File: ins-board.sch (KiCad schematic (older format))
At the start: 83 parts, among them Q1 FDN306P, U2 STM32F415RGT6, U6 LT1761-3.3, U7 LT1965, X1 CRYSTAL 16MHz 10ppm

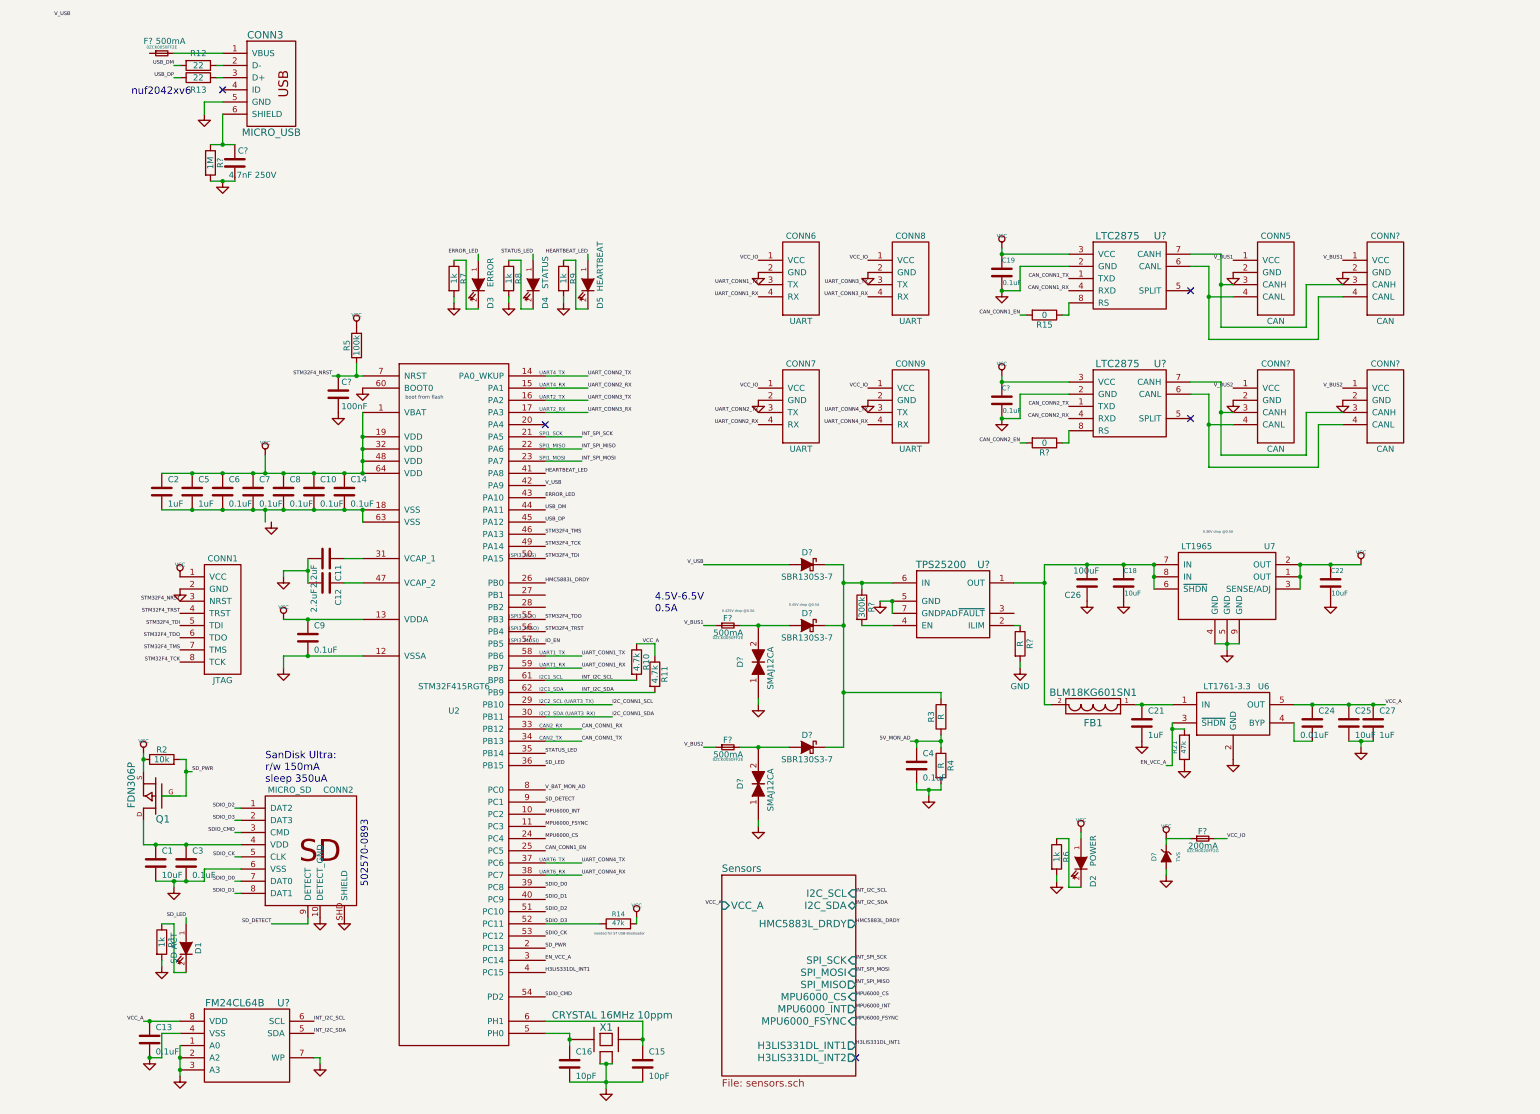
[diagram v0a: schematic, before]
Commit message: smaller esd protection
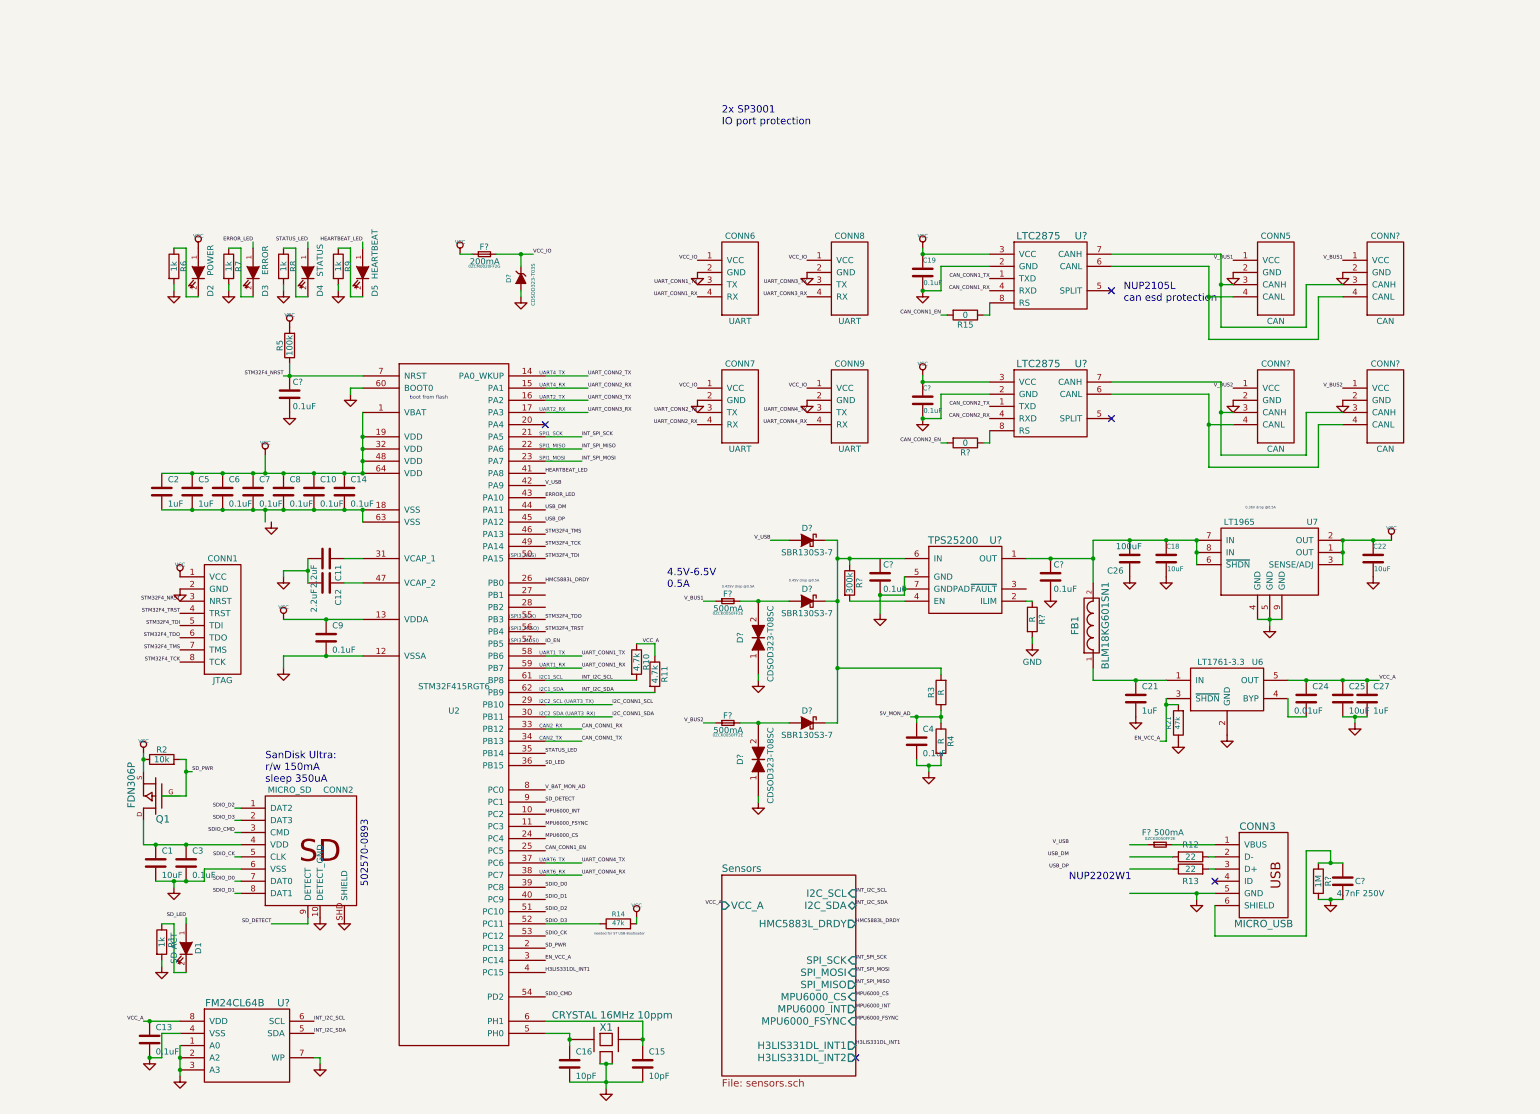
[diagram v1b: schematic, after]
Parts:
- removed D?: TVS, symbol ZENERsmall
- added C? (x2): 0.1uF, symbol C
- added D?: CDSOD323-T03S, symbol ZENERsmall
- C?: value 100nF -> 0.1uF
- D? (x2): value SMAJ12CA -> CDSOD323-T08SC
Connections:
- net GND: now also C?.2, C?.2, D?.1 (A)
- net USB_DM: no longer R12.2
- net USB_DP: no longer R13.1
- net VCC_IO: now also D?.2 (K)
- net at C18.1, C26.2, FB1.2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: now also C?.1
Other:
- note added: "2x SP3001\nIO port protection"
- note added: "NUP2105L \ncan esd protection"
- note added: "NUP2202W1"
- note removed: "nuf2042xv6"
- moved on the sheet: C18, C19, C21, C22, C24, C25, C26, C27, C4, C9, C?, CONN3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

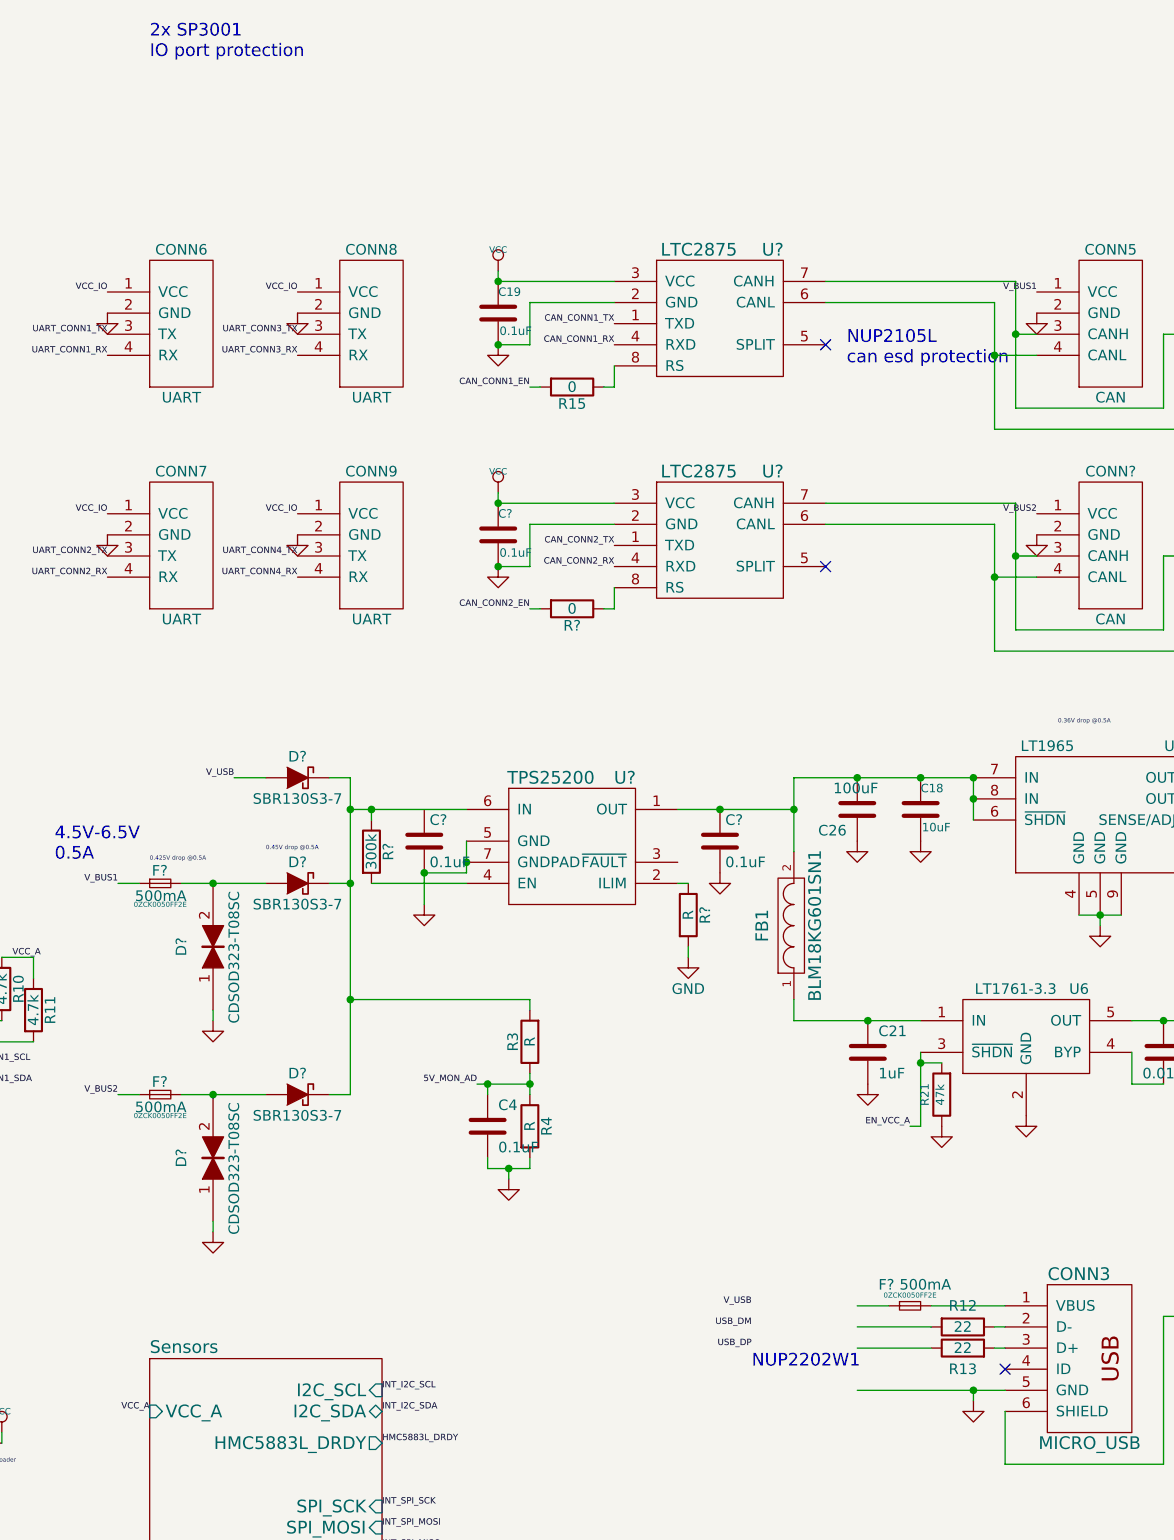
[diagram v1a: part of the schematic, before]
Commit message: USB ESD protection
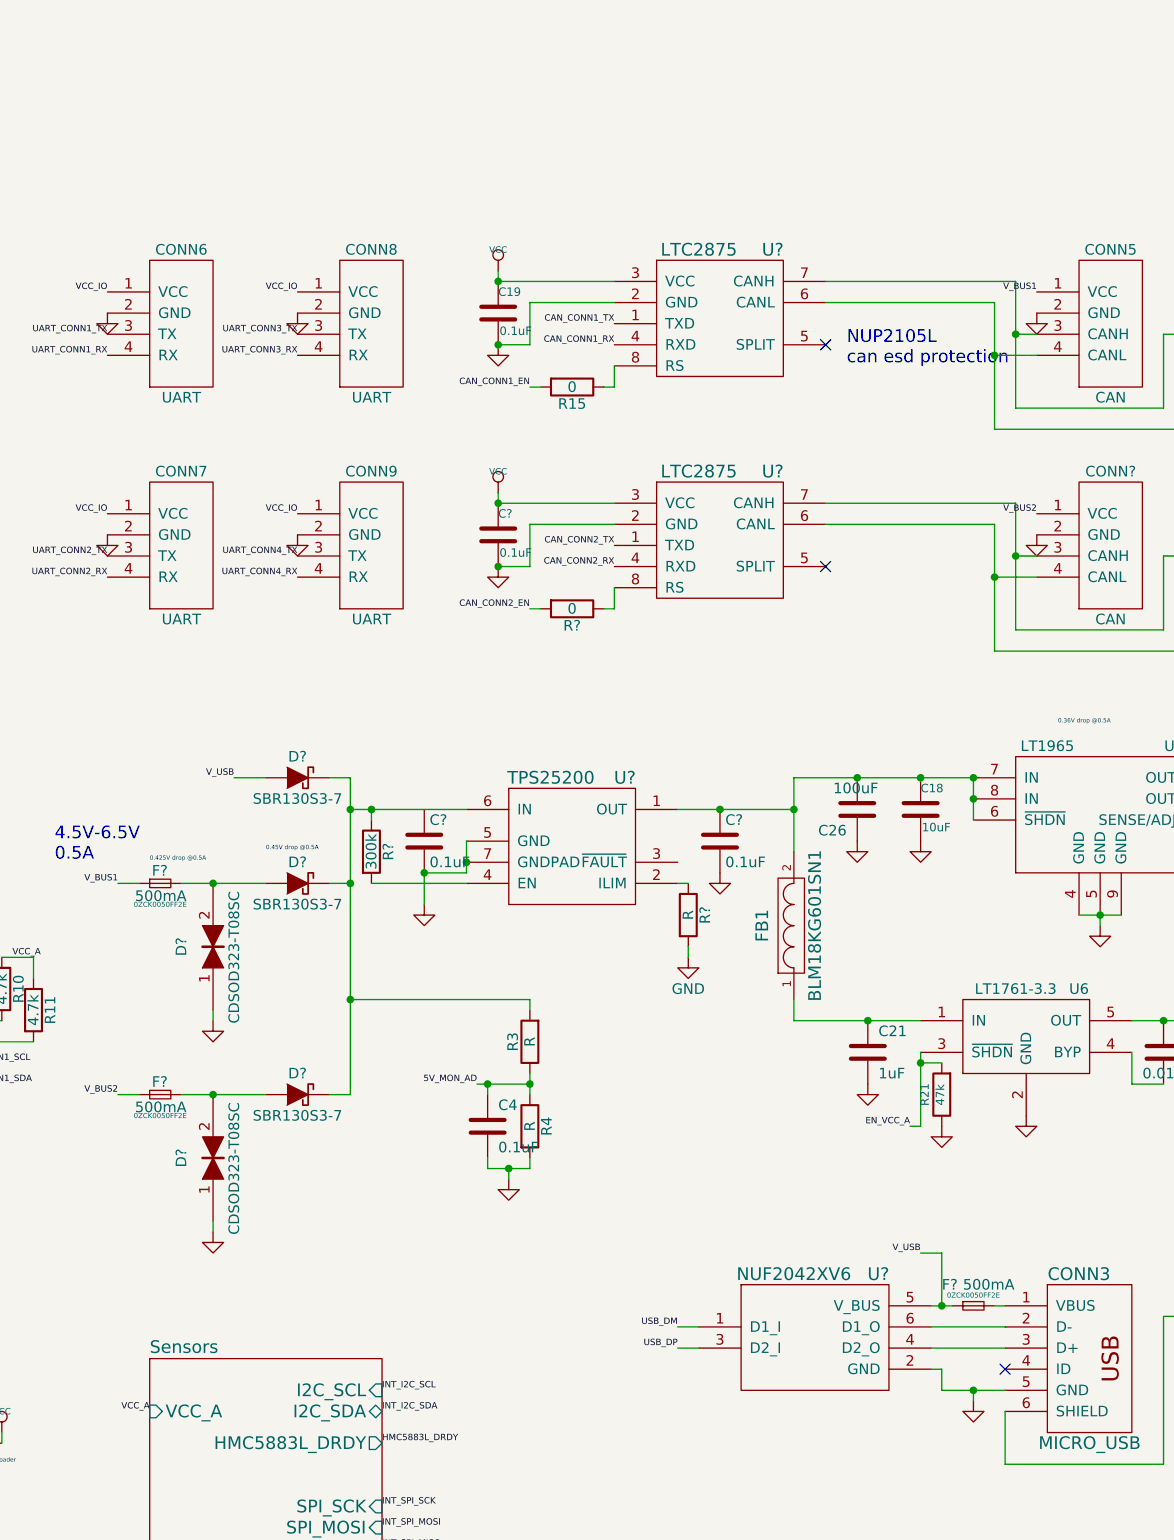
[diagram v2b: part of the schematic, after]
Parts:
- removed R12, R13: 22, symbol R
- added U?: NUF2042XV6, symbol NUF2042XV6
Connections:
- net GND: now also U?.2 (GND)
- net USB_DM: now also U?.1 (D1_I)
- net USB_DP: now also U?.3 (D2_I)
- net V_USB: now also F?.1, U?.5 (V_BUS)
- net at CONN3.2 (D-): now also U?.6 (D1_O)
- net at CONN3.3 (D+): now also U?.4 (D2_O)
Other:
- note removed: "2x SP3001\nIO port protection"
- note removed: "NUP2202W1"
- moved on the sheet: F?
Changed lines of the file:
@@
 Text Label 10800 4300 0    30   ~ 0
 VCC_A
-$Comp
-L R R13
-U 1 1 517DA7DC
-P 9250 5850
-F 0 "R13" V 9150 5850 50  0000 C CNN
-F 1 "22" V 9250 5850 50  0000 C CNN
-F 2 "" H 9250 5850 60  0001 C CNN
-F 3 "" H 9250 5850 60  0001 C CNN
-	1    9250 5850
-	0    -1   -1   0
-$EndComp
-$Comp
-L R R12
-U 1 1 517DA7D3
-P 9250 5750
-F 0 "R12" V 9150 5750 50  0000 C CNN
-F 1 "22" V 9250 5750 50  0000 C CNN
-F 2 "" H 9250 5750 60  0001 C CNN
-F 3 "" H 9250 5750 60  0001 C CNN
-	1    9250 5750
-	0    1    1    0
-$EndComp
 Text Label 3950 2700 0    30   ~ 0
 V_USB
@@
 Text Label 5800 3150 2    30   ~ 0
 V_USB
-Text Label 8250 5650 2    30   ~ 0
+Text Label 9050 5400 2    30   ~ 0
 V_USB
 Text Label 3950 2900 0    30   ~ 0
@@
 Text Label 3950 3000 0    30   ~ 0
 USB_DP
-Text Label 8250 5850 2    30   ~ 0
+Text Label 7900 5850 2    30   ~ 0
 USB_DP
-Text Label 8250 5750 2    30   ~ 0
+Text Label 7900 5750 2    30   ~ 0
 USB_DM
 $Comp
@@
 L F_Small F?
 U 1 1 55398896
-P 9000 5650
-F 0 "F?" H 8850 5750 50  0000 L CNN
-F 1 "500mA" H 8950 5750 50  0000 L CNN
-F 2 "" H 9000 5650 60  0000 C CNN
-F 3 "" H 9000 5650 60  0000 C CNN
-F 4 "0ZCK0050FF2E" H 9000 5700 24  0000 C CNN "Part"
-	1    9000 5650
+P 9300 5650
+F 0 "F?" H 9150 5750 50  0000 L CNN
+F 1 "500mA" H 9250 5750 50  0000 L CNN
+F 2 "" H 9300 5650 60  0000 C CNN
+F 3 "" H 9300 5650 60  0000 C CNN
+F 4 "0ZCK0050FF2E" H 9300 5700 24  0000 C CNN "Part"
+	1    9300 5650
 	1    0    0    -1
 $EndComp
@@
 	4450 7600 4750 7600
 Wire Wire Line
-	9100 5650 9450 5650
+	9400 5650 9450 5650
 Wire Wire Line
 	2450 2600 2300 2600
@@
 	9300 6100 9300 6050
 Wire Wire Line
-	8750 6050 9300 6050
+	9150 6050 9300 6050
 Wire Wire Line
 	9300 6050 9450 6050
@@
 	9500 2450 10200 2450
 Wire Wire Line
-	9400 5750 9450 5750
-Wire Wire Line
-	9400 5850 9450 5850
-Wire Wire Line
-	8750 5750 9100 5750
-Wire Wire Line
-	8750 5850 9100 5850
+	9100 5750 9450 5750
+Wire Wire Line
+	9100 5850 9450 5850
 Wire Wire Line
 	7600 1200 7600 1300
@@
 	7050 750  7050 800
 Wire Wire Line
-	6900 3600 6900 3550
-Wire Wire Line
-	6900 3550 6900 3450
+	6900 3450 6900 3550
+Wire Wire Line
+	6900 3550 6900 3600
 Wire Wire Line
 	6450 3650 6900 3650
@@
 	10400 5700 10400 5800
 Connection ~ 10400 5800
-Wire Wire Line
-	8900 5650 8750 5650
 Connection ~ 9300 6050
 Wire Wire Line
@@
 Wire Wire Line
 	10200 5700 10400 5700
-Text Notes 5400 -250 0    60   ~ 0
-2x SP3001\nIO port protection
 Wire Wire Line
 	3550 800  3750 800
@@
 Wire Wire Line
 	2350 1900 2350 1950
-Text Notes 8250 5950 0    60   ~ 0
-NUP2202W1
 $Comp
 L C C?
@@
 Connection ~ 8450 3300
 Wire Wire Line
-	6700 3600 6900 3600
+	6900 3600 6700 3600
 Wire Wire Line
 	6700 3600 6700 3750
@@
 Wire Wire Line
 	3750 1150 3750 1100
+$Comp
+L NUF2042XV6 U?
+U 1 1 55450335
+P 8550 5800
+F 0 "U?" H 8850 6100 60  0000 C CNN
+F 1 "NUF2042XV6" H 8450 6100 60  0000 C CNN
+F 2 "" H 8550 5700 60  0000 C CNN
+F 3 "" H 8550 5700 60  0000 C CNN
+	1    8550 5800
+	1    0    0    -1
+$EndComp
+Wire Wire Line
+	9150 6050 9150 5950
+Wire Wire Line
+	9150 5950 9100 5950
+Wire Wire Line
+	9100 5650 9150 5650
+Wire Wire Line
+	9150 5650 9200 5650
+Wire Wire Line
+	7900 5750 8000 5750
+Wire Wire Line
+	7900 5850 8000 5850
+Wire Wire Line
+	9150 5650 9150 5400
+Wire Wire Line
+	9150 5400 9050 5400
+Connection ~ 9150 5650
 $EndSCHEMATC
